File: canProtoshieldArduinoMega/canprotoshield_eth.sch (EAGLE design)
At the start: 58 parts, among them CN1 1X4-3.5MM, CN10 1X4-3.5MM, CN11 1X4-3.5MM, CN12 1X4-3.5MM, CN13 1X4-3.5MM, CN14 1X4-3.5MM, CN15 1X4-3.5MM, CN16 1X4-3.5MM, CN17 1X4-3.5MM, CN18 1X4-3.5MM, CN19 1X4-3.5MM, CN2 1X4-3.5MM, CN20 1X4-3.5MM, CN21 1X4-3.5MM, CN22 1X4-3.5MM, CN23 1X4-3.5MM, CN24 1X4-3.5MM, CN25 1X4-3.5MM, CN26 1X4-3.5MM, CN27 1X4-3.5MM, CN28 1X4-3.5MM, CN29 1X4-3.5MM, CN3 1X4-3.5MM, CN30 1X4-3.5MM, CN31 1X4-3.5MM, CN32 1X4-3.5MM, CN33 1X4-3.5MM, CN34 1X4-3.5MM, CN4 1X4-3.5MM, CN5 1X4-3.5MM, CN6 1X4-3.5MM, CN7 1X4-3.5MM, CN8 1X4-3.5MM, CN9 1X4-3.5MM, Q1 16mhz, U2 MCP2551, U3 ARDUINO-MEGAFULL

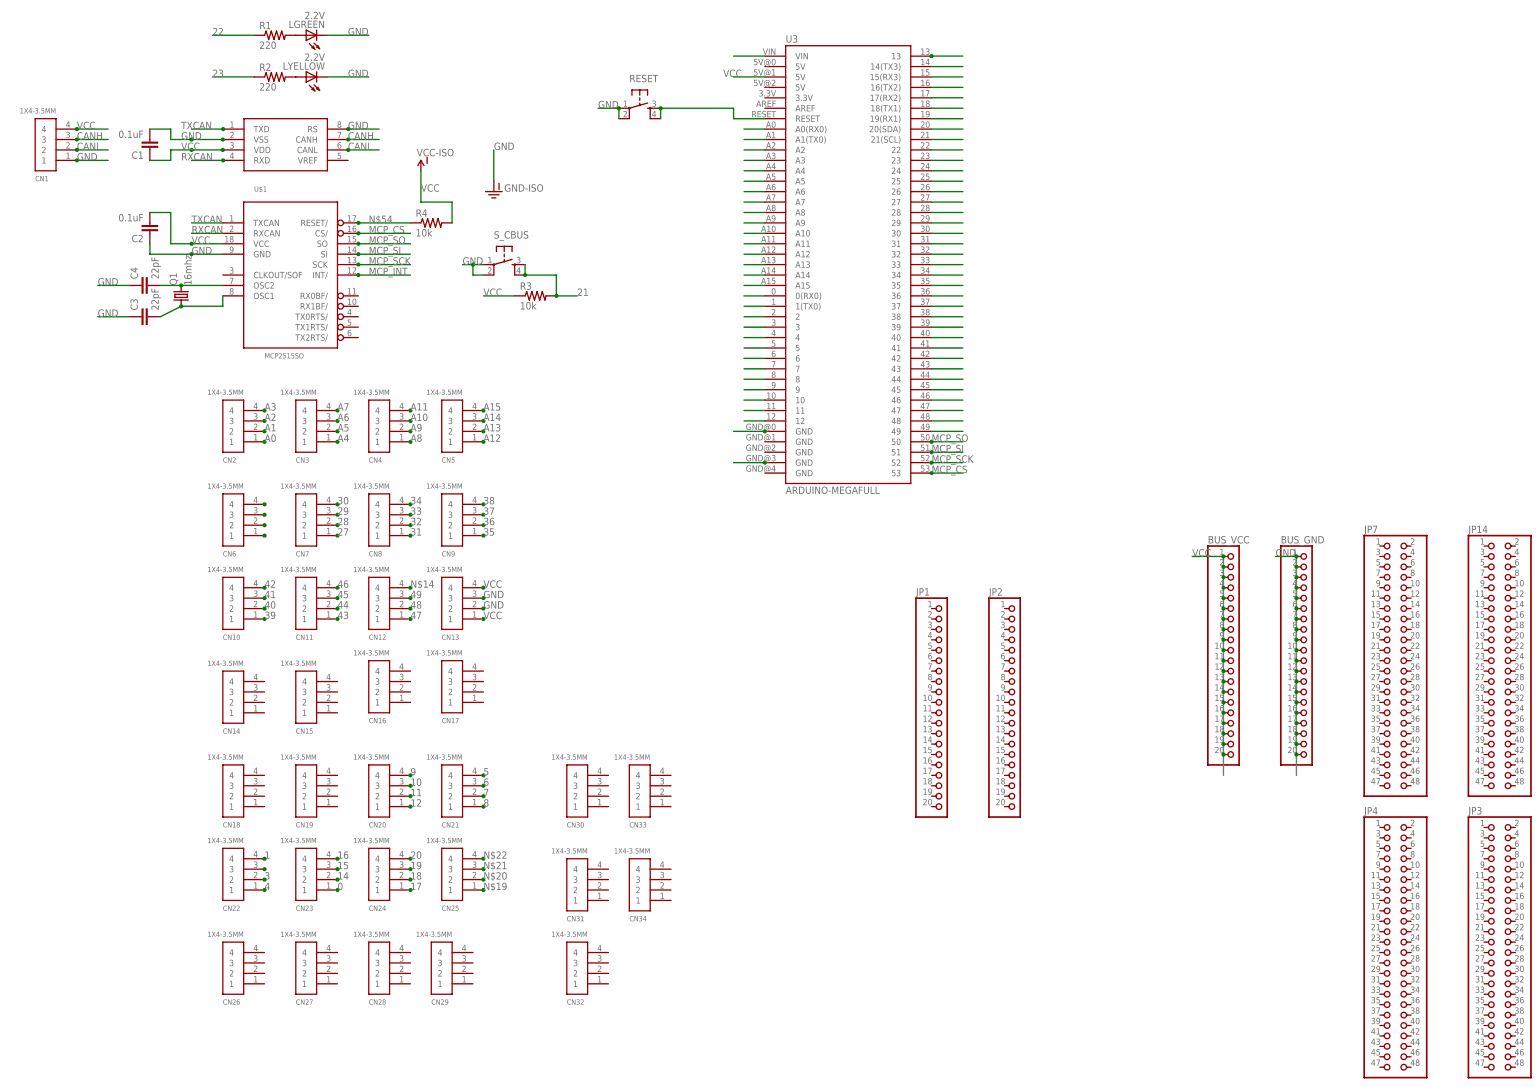
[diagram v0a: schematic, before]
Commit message: Ethernet connector-previous version
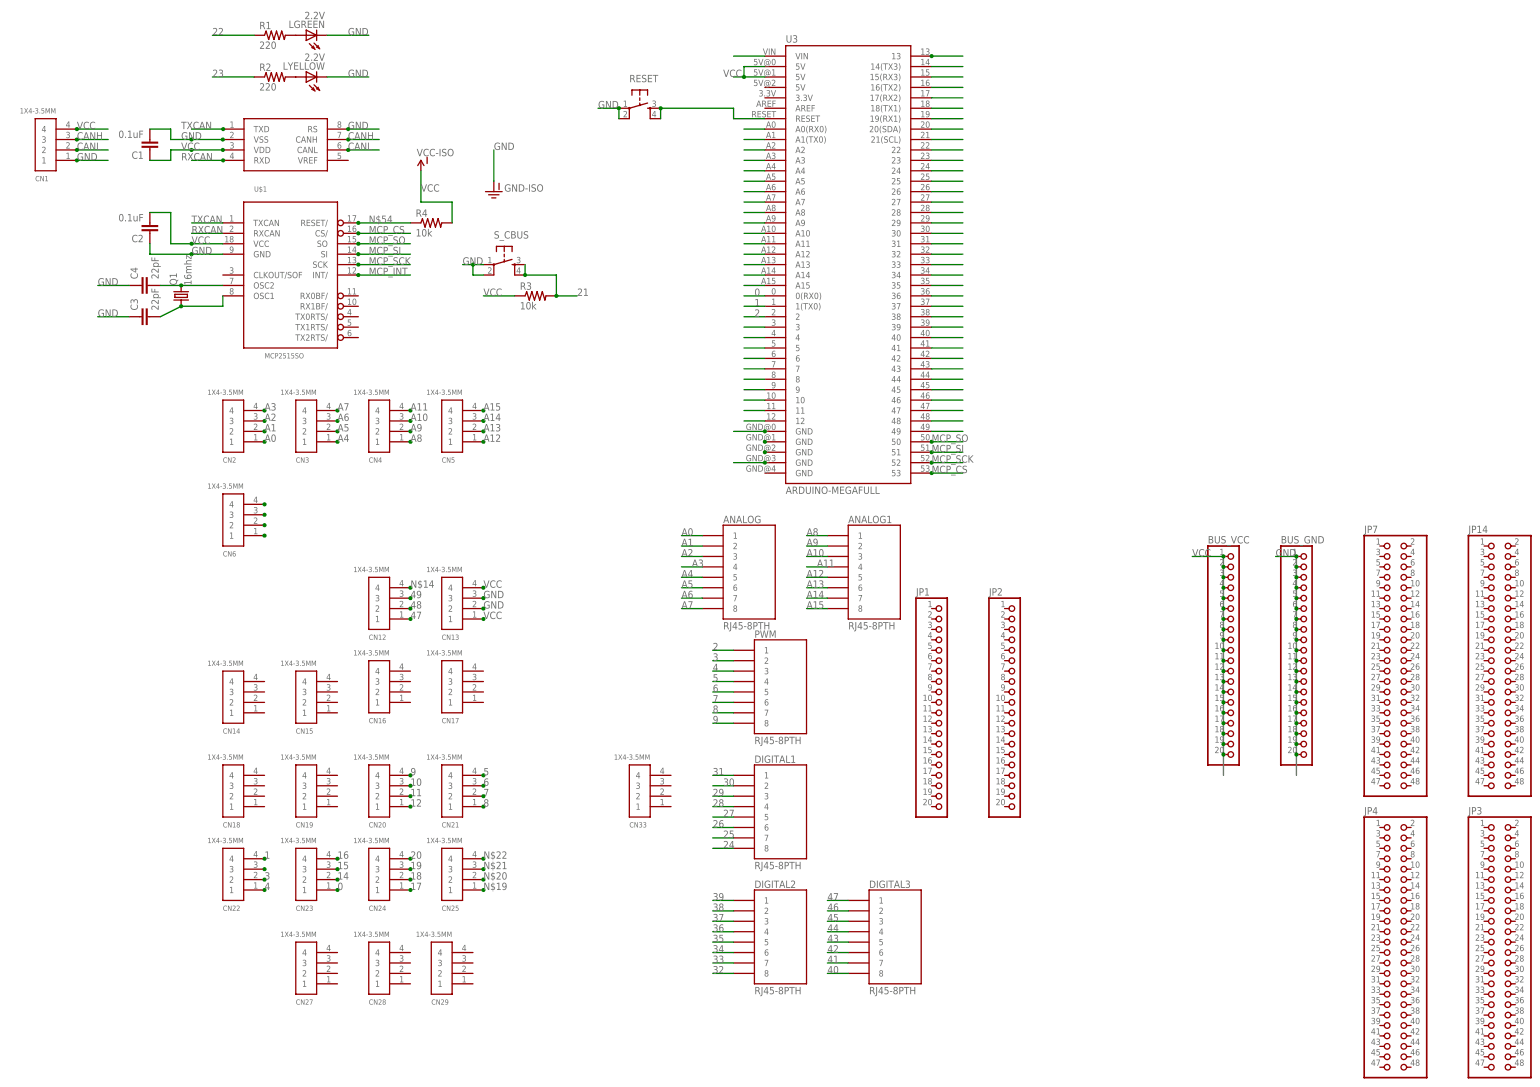
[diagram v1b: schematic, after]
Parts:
- removed CN10, CN11, CN26, CN30, CN31, CN32, CN34, CN7, CN8, CN9: 1X4-3.5MM, Arduino_merg:1X4-3.5MM
- added ANALOG, ANALOG1, DIGITAL1, DIGITAL2, DIGITAL3, PWM: RJ45-8PTH, SparkFun-Connectors:RJ45-8PTH
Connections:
- new net N$55: U3.GND@1
- new net N$56: U3.GND@2
- net 2: now also PWM.1
- net 24: now also DIGITAL1.8
- net 25: now also DIGITAL1.7
- net 26: now also DIGITAL1.6
- net 27: now also DIGITAL1.5; no longer CN7.1
- net 28: now also DIGITAL1.4; no longer CN7.2
- net 29: now also DIGITAL1.3; no longer CN7.3
- net 3: now also PWM.2
- net 30: now also DIGITAL1.2; no longer CN7.4
- net 31: now also DIGITAL1.1; no longer CN8.1
- net 32: now also DIGITAL2.8; no longer CN8.2
- net 33: now also DIGITAL2.7; no longer CN8.3
- net 34: now also DIGITAL2.6; no longer CN8.4
- net 35: now also DIGITAL2.5; no longer CN9.1
- net 36: now also DIGITAL2.4; no longer CN9.2
- net 37: now also DIGITAL2.3; no longer CN9.3
- net 38: now also DIGITAL2.2; no longer CN9.4
- net 39: now also DIGITAL2.1; no longer CN10.1
- net 4: now also PWM.3
- net 40: now also DIGITAL3.8; no longer CN10.2
- net 41: now also DIGITAL3.7; no longer CN10.3
- net 42: now also DIGITAL3.6; no longer CN10.4
- net 43: now also DIGITAL3.5; no longer CN11.1
- net 44: now also DIGITAL3.4; no longer CN11.2
- net 45: now also DIGITAL3.3; no longer CN11.3
- net 46: now also DIGITAL3.2; no longer CN11.4
- net 47: now also DIGITAL3.1
- net 5: now also PWM.4
- net 6: now also PWM.5
- net 7: now also PWM.6
- net 8: now also PWM.7
- net 9: now also PWM.8
- net A0: now also ANALOG.1
- net A1: now also ANALOG.2
- net A10: now also ANALOG1.3
- net A11: now also ANALOG1.4
- net A12: now also ANALOG1.5
- net A13: now also ANALOG1.6
- net A14: now also ANALOG1.7
- net A15: now also ANALOG1.8
- net A2: now also ANALOG.3
- net A3: now also ANALOG.4
- net A4: now also ANALOG.5
- net A5: now also ANALOG.6
- net A6: now also ANALOG.7
- net A7: now also ANALOG.8
- net A8: now also ANALOG1.1
- net A9: now also ANALOG1.2
- net VCC: now also U3.5V@0

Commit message: Board with ethernet connectors.
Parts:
- removed CN33, CN6: 1X4-3.5MM, Arduino_merg:1X4-3.5MM
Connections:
- removed net N$53: CN6.4
- net 24: no longer CN6.3
- net 25: no longer CN6.2
- net 26: no longer CN6.1
- net GND: now also U3.GND@4
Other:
- moved on the sheet: CN12, CN13, CN14, CN15, CN16, CN17, CN18, CN19, CN20, CN21, CN22, CN23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
